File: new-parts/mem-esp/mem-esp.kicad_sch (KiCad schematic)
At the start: 70 parts, among them J1 Conn_02x02_Odd_Even, J2 BHR-10-VUA, J3 BHR-10-VUA, J4 Conn_01x01, J5 Conn_01x01, J6 Conn_01x01, J7 Conn_01x01, J8 BHR-10-VUA, U1 BA7806CP-E2, U2 ESP32-S3-DevKitC, U3 LTV-247, U4 LTV-247, U5 DRV8908, U6 LTV-247, U7 LTV-247, U8 LTV-247, U9 DRV8908

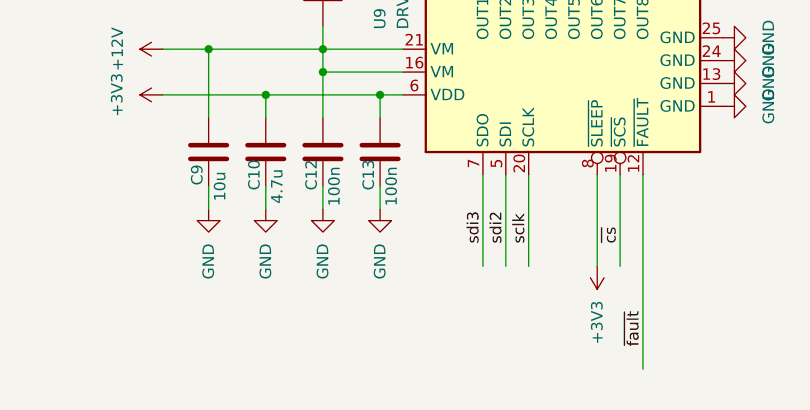
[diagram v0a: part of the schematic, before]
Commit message: mem-esp: Add solder jumper to connect SPI if the second driver is not populated.
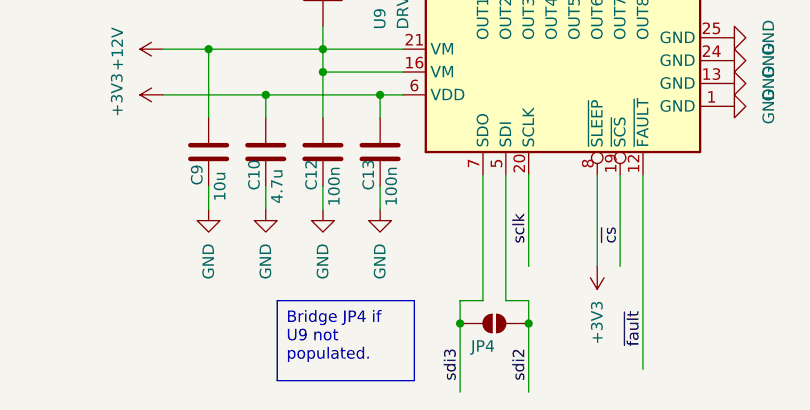
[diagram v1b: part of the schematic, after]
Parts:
- added JP4: SolderJumper_2_Open, Jumper:SolderJumper-2_P1.3mm_Open_TrianglePad1.0x1.5mm, symbol Jumper:SolderJumper_2_Open
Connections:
- net sdi2: now also JP4.2 (B)
- net sdi3: now also JP4.1 (A)
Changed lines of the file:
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@@
 	)
 	(junction
+		(at 270.51 256.54)
+		(diameter 0)
+		(color 0 0 0 0)
+	)
+	(junction
 		(at 218.44 27.94)
 		(diameter 0)
@@
 	)
 	(junction
+		(at 262.89 256.54)
+		(diameter 0)
+		(color 0 0 0 0)
+	)
+	(junction
 		(at 123.19 36.83)
 		(diameter 0)
@@
 	(wire
 		(pts
+			(xy 270.51 256.54) (xy 270.51 254)
+		)
+		(stroke
+			(width 0)
+			(type default)
+		)
+	)
+	(wire
+		(pts
 			(xy 369.57 74.93) (xy 369.57 38.1)
 		)
@@
 	(wire
 		(pts
+			(xy 262.89 256.54) (xy 262.89 254)
+		)
+		(stroke
+			(width 0)
+			(type default)
+		)
+	)
+	(wire
+		(pts
 			(xy 166.37 116.84) (xy 179.07 116.84)
 		)
@@
 	(wire
 		(pts
+			(xy 270.51 256.54) (xy 270.51 264.16)
+		)
+		(stroke
+			(width 0)
+			(type default)
+		)
+	)
+	(wire
+		(pts
 			(xy 275.59 217.17) (xy 275.59 205.74)
 		)
@@
 	(wire
 		(pts
-			(xy 265.43 250.19) (xy 265.43 240.03)
-		)
-		(stroke
-			(width 0)
-			(type default)
-		)
-	)
-	(wire
-		(pts
 			(xy 293.37 184.15) (xy 295.91 184.15)
 		)
@@
 	(wire
 		(pts
+			(xy 265.43 240.03) (xy 265.43 254)
+		)
+		(stroke
+			(width 0)
+			(type default)
+		)
+	)
+	(wire
+		(pts
 			(xy 247.65 223.52) (xy 247.65 226.06)
 		)
@@
 	(wire
 		(pts
-			(xy 267.97 250.19) (xy 267.97 240.03)
-		)
-		(stroke
-			(width 0)
-			(type default)
-		)
-	)
-	(wire
-		(pts
 			(xy 328.93 134.62) (xy 328.93 137.16)
 		)
@@
 	(wire
 		(pts
+			(xy 270.51 254) (xy 267.97 254)
+		)
+		(stroke
+			(width 0)
+			(type default)
+		)
+	)
+	(wire
+		(pts
+			(xy 262.89 256.54) (xy 262.89 264.16)
+		)
+		(stroke
+			(width 0)
+			(type default)
+		)
+	)
+	(wire
+		(pts
 			(xy 207.01 43.18) (xy 218.44 43.18)
 		)
@@
 	(wire
 		(pts
+			(xy 267.97 240.03) (xy 267.97 254)
+		)
+		(stroke
+			(width 0)
+			(type default)
+		)
+	)
+	(wire
+		(pts
 			(xy 257.81 53.34) (xy 254 53.34)
 		)
@@
 	(wire
 		(pts
+			(xy 262.89 254) (xy 265.43 254)
+		)
+		(stroke
+			(width 0)
+			(type default)
+		)
+	)
+	(wire
+		(pts
 			(xy 328.93 27.94) (xy 341.63 27.94)
 		)
@@
 		)
 	)
+	(text_box "Bridge JP4 if U9 not populated."
+		(exclude_from_sim no)
+		(at 242.57 254 0)
+		(size 15.24 8.89)
+		(stroke
+			(width 0)
+			(type default)
+		)
+		(fill
+			(type none)
+		)
+		(effects
+			(font
+				(size 1.27 1.27)
+			)
+			(justify left top)
+		)
+	)
 	(text_box "We supply 6V to the ESP to make sure that it does *not* draw power through its USB ports. The USB ports are protected by diodes (D1 and D7 on the ESP board) against reverse current."
 		(exclude_from_sim no)
@@
 		)
 	)
-	(label "sdi2"
-		(at 267.97 247.65 90)
-		(fields_autoplaced yes)
-		(effects
-			(font
-				(size 1.27 1.27)
-			)
-			(justify left bottom)
-		)
-	)
 	(label "a5"
 		(at 170.18 114.3 0)
@@
 		)
 	)
-	(label "sdi3"
-		(at 265.43 247.65 90)
-		(fields_autoplaced yes)
-		(effects
-			(font
-				(size 1.27 1.27)
-			)
-			(justify left bottom)
-		)
-	)
 	(label "in1"
 		(at 207.01 43.18 0)
@@
 		)
 	)
+	(label "sdi3"
+		(at 262.89 262.89 90)
+		(fields_autoplaced yes)
+		(effects
+			(font
+				(size 1.27 1.27)
+			)
+			(justify left bottom)
+		)
+	)
 	(label "in4"
 		(at 207.01 88.9 0)
@@
 		)
 	)
+	(label "sdi2"
+		(at 270.51 262.89 90)
+		(fields_autoplaced yes)
+		(effects
+			(font
+				(size 1.27 1.27)
+			)
+			(justify left bottom)
+		)
+	)
 	(label "in2"
 		(at 207.01 58.42 0)
@@
 				)
 			)
+		)
+	)
+	(symbol
+		(lib_id "Jumper:SolderJumper_2_Open")
+		(at 266.7 256.54 0)
+		(unit 1)
+		(exclude_from_sim yes)
+		(in_bom no)
+		(on_board yes)
+		(dnp no)
+		(property "Reference" "JP4"
+			(at 265.43 259.08 0)
+			(effects
+				(font
+					(size 1.27 1.27)
+				)
+			)
+		)
+		(property "Value" "SolderJumper_2_Open"
+			(at 266.7 252.73 0)
+			(effects
+				(font
+					(size 1.27 1.27)
+				)
+				(hide yes)
+			)
+		)
+		(property "Footprint" "Jumper:SolderJumper-2_P1.3mm_Open_TrianglePad1.0x1.5mm"
+			(at 266.7 256.54 0)
+			(effects
+				(font
+					(size 1.27 1.27)
+				)
+				(hide yes)
+			)
+		)
+		(property "Datasheet" "~"
+			(at 266.7 256.54 0)
+			(effects
+				(font
+					(size 1.27 1.27)
+				)
+				(hide yes)
+			)
+		)
+		(property "Description" "Solder Jumper, 2-pole, open"
+			(at 266.7 256.54 0)
+			(effects
+				(font
+					(size 1.27 1.27)
+				)
+				(hide yes)
+			)
+		)
+		(pin "2"
+		)
+		(pin "1"
+		)
+		(instances
+			(project "mem-esp"
+				(path "/8e7358e7-c3ef-4f3e-9154-e7eba01c544e"
+					(reference "JP4")
+					(unit 1)
+				)
+			)
